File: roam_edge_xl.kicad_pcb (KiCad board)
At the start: 6 copper layers, 103 x 60 mm, 231 parts, among them IC4 MAX13487EESA+T, J1 Battery, J11 Conn_01x05_Pin, J2 USB_B_Micro, J3 IPEX, J4 USB_B_Micro, J5 DNP, J6 CA-L01, J7 SIM8060-6-0-14-00-A, J8 MX23A18NF1, J9 Conn_01x11_Pin, Q4 Q_NPN_BEC_BRT, Q5 Q_NPN_BEC_BRT, Q6 Q_NPN_BEC_BRT, Q7 2N7002E, Q9 AO4407A, SW1 SW_Push, SW2 SW_Push, U1 NUP4202, U10 LP5907MFX-3.3, U11 TXB0108RGY, U12 CN809T, U13 LIS2DH12TR, U15 LM66100DCKR, U16 LM66100DCKR, U18 TPS61022, U19 LTV-217, U2 TXB0102DCU, U20 LC760Z, U21 LP5907MFX-3.3, U22 TP4056, U25 ESP32-S3-MINI-1, U26 TJA1051T/3, U27 LP5907MFX-3.3, U28 USBLC6-2SC6, U3 TPS566242DRLR, U4 EG1192L, U5 LTV-217, U6 W25Q128JVP, U7 EG915UEUAC-N05-SNNSA, U8 USBLC6-2SC6, U9 SQS201CENW-T1_GE3

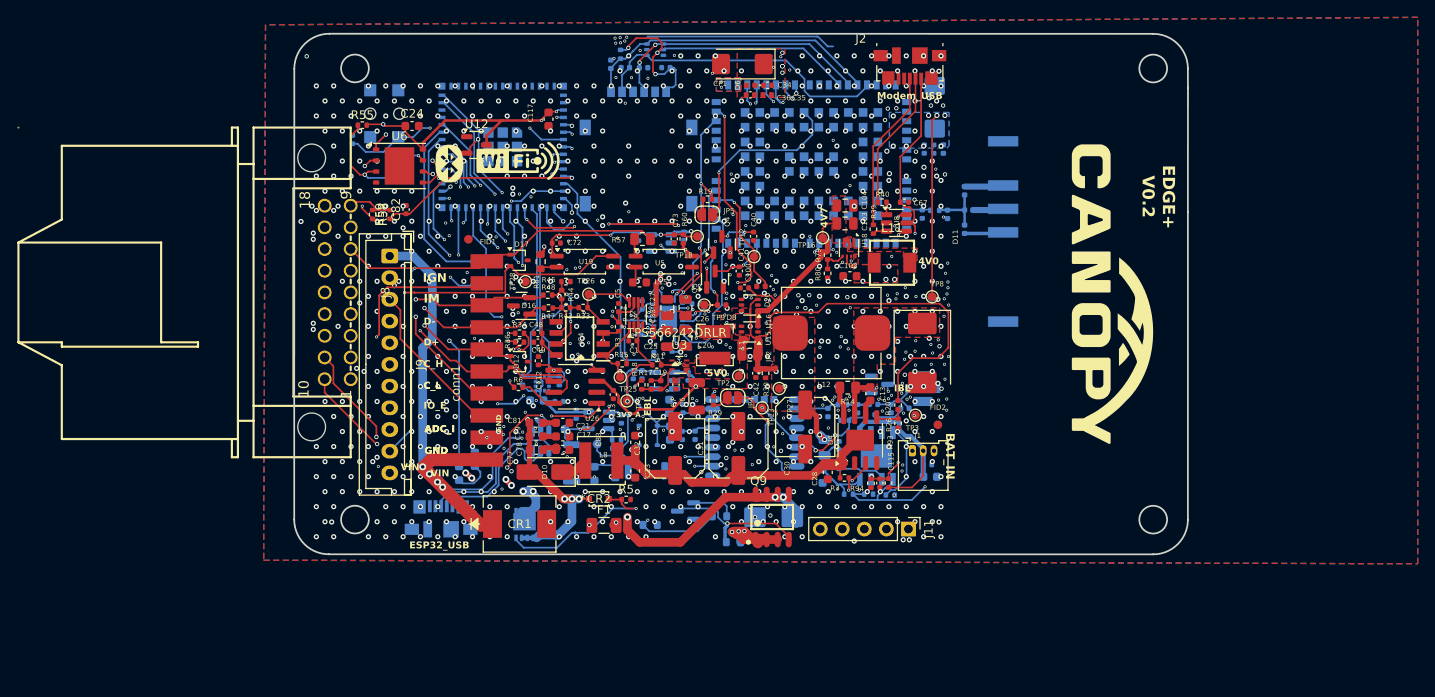
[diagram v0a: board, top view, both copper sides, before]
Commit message: updated Tamper switch design
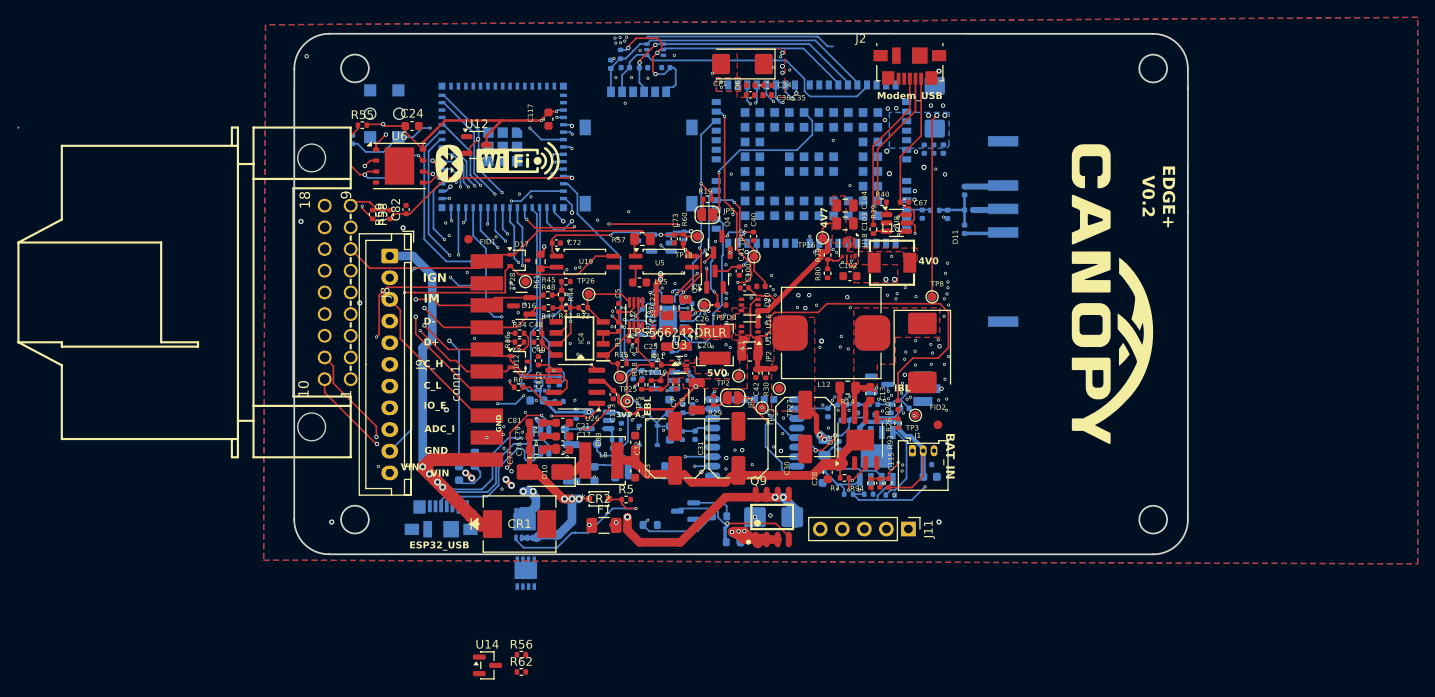
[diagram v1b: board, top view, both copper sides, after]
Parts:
- added Q1: SQS201CENW-T1_GE3, PMOS_SQS201CENW:PDFN3333-8_L3.1-W3.2-P0.65-LS3.4-BL, B.Cu at (55.1, 109.3)
- added R56: 10K, Resistor_SMD:R_0402_1005Metric, F.Cu at (54.6, 118.7)
- added R62: 4.7K, Resistor_SMD:R_0402_1005Metric, F.Cu at (54.6, 120.7)
- added U14: CN809L, Package_TO_SOT_SMD:SOT-23, F.Cu at (50.7, 119.9)
- S1: footprint limit switch:SW-SMD_ESE11MV9T -> Tamper_Switch:ESE11MV9
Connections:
- CR2 pad 2: Net-(U9-G) -> Net-(Q1-G)
- R5 pad 1: Net-(U9-G) -> Net-(Q1-G)
- U9 pad 4: Net-(U9-G) -> unconnected-(U9-G-Pad4)
- U9 pad 5: Net-(F1-Pad2) -> Net-(U9-D-Pad5)
- U9 pad 6: Net-(F1-Pad2) -> Net-(U9-D-Pad5)
- U9 pad 7: Net-(F1-Pad2) -> Net-(U9-D-Pad5)
- U9 pad 8: Net-(F1-Pad2) -> Net-(U9-D-Pad5)
- U9 pad 9: Net-(F1-Pad2) -> Net-(U9-D-Pad5)
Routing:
- net Net-(U9-G): track 20.3 -> 0.00 mm, vias 1 -> 0
- net V_EXT_P: track 91.1 -> 111.4 mm, vias 6 -> 7
- net GND: vias 1010 -> 205

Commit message: modified the antenna routing
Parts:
- added C101: 100nF, Capacitor_SMD:C_0402_1005Metric, B.Cu at (94.7, 92.8)
- C116: value 24pf -> 100pf
- L6: value 51nH -> 68nH
- R4: value 10 -> 0
- moved U9 10.5 mm to (47.6, 111.1)
- moved R86 5.91 mm to (95.6, 100.7), turned to 0 degrees
- moved Q1 5.80 mm to (54.9, 103.5)
- moved C2 4.30 mm to (96.1, 92.8), turned to -90 degrees
- moved C110 3.82 mm to (90.5, 98.3)
- moved J3 2.36 mm to (101.1, 90.4)
- moved L6 2.25 mm to (97.1, 91.7), turned to 90 degrees
- moved R4 2.16 mm to (93.1, 92.3)
- moved D13 1.38 mm to (95.9, 89.9), turned to -90 degrees
- moved U22 1.37 mm to (95.1, 97.1), turned to 0 degrees
- moved C109 1.28 mm to (100.9, 99.2), turned to -90 degrees
- moved R85 1.16 mm to (93.6, 100.7)
- moved R2 1.00 mm to (98.0, 100.7), turned to 0 degrees
- moved C116 0.95 mm to (94.4, 90.4)
- moved L13 0.88 mm to (90.0, 89.9), turned to -90 degrees
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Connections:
- C2 pad 1: 3V3_ANT -> Net-(C101-Pad1)
- L6 pad 1: Net-(L6-Pad1) -> Net-(C101-Pad1)
- R4 pad 1: Net-(L6-Pad1) -> Net-(C101-Pad1)
- S1 pad 2: GND -> /LID_OPEN_DET
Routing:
- net Net-(Q1-G): track 0.00 -> 20.6 mm, vias 0 -> 1
- net V_EXT_P: track 111.4 -> 91.1 mm, vias 7 -> 6
- net 5V0_BUCK: track 146.8 -> 137.6 mm, vias 11 -> 9
- net Net-(U22-CE): track 9.36 -> 2.01 mm
- net VBAT: track 46.0 -> 41.2 mm
- net Net-(L6-Pad1): track 3.72 -> 0.00 mm
- net Net-(C101-Pad1): track 0.00 -> 3.55 mm
- net 3V3_ANT: track 16.3 -> 12.9 mm, vias 3 -> 1
- net /NTC: track 18.3 -> 21.6 mm, vias 1 -> 0
- net Net-(U22-VCC): track 10.5 -> 7.21 mm
- net Net-(U4-EN): track 5.37 -> 2.91 mm, vias 2 -> 0
- net Net-(J6-Pad2): track 2.88 -> 4.49 mm
- net Net-(J6-Pad3): track 1.91 -> 3.50 mm
- net /IBL: track 68.7 -> 69.8 mm
- net /CHG_EN: track 71.0 -> 72.1 mm
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- added copper zone on B.Cu, net Net-(U22-VCC)
